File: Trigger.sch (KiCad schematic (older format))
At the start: 32 parts, among them J1 USB_B_Micro, J2 TP1, J3 Conn_01x04_IO, J4 Screw_Terminal_01x06, J5 Conn_01x05_Male, Q1 Q_NMOS_GSD, SW2 SW_Push, U1 MCP6002, U2 SAMD21E, U3 TPS769XX

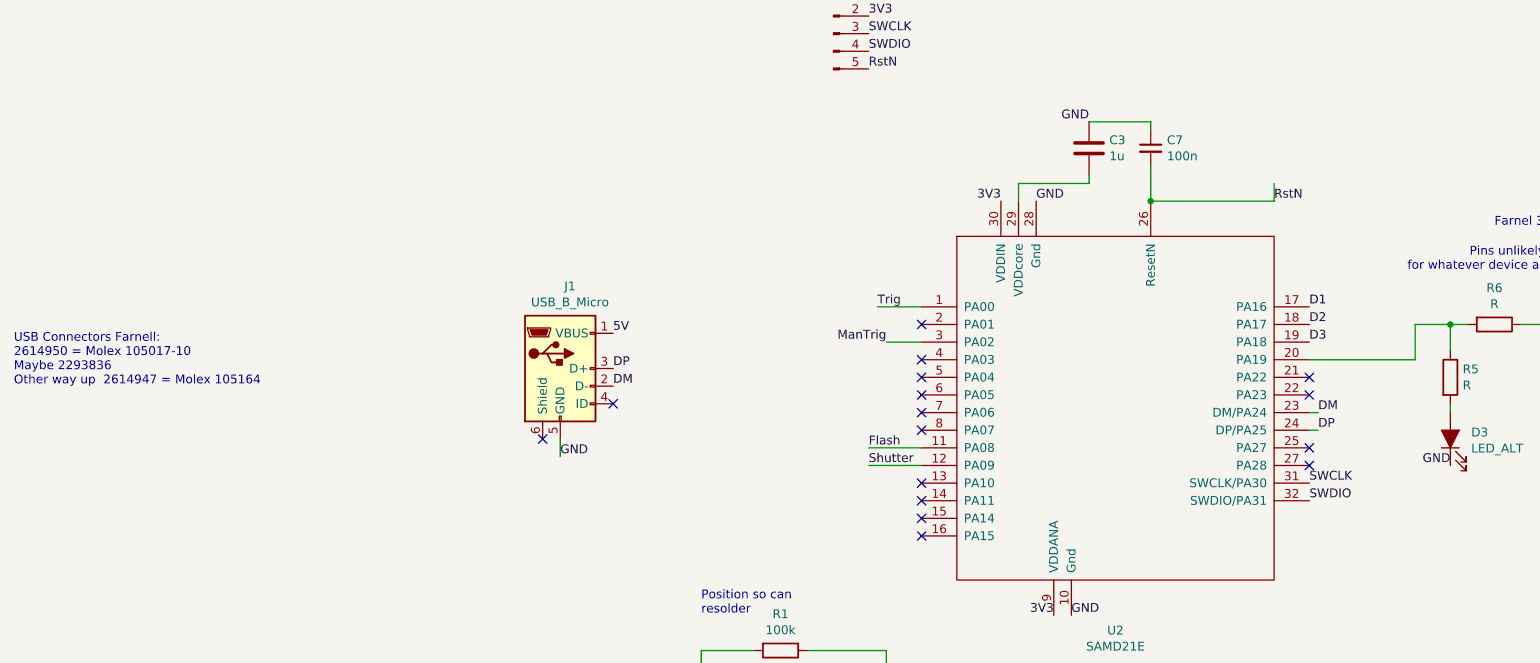
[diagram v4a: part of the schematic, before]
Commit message: Layout on board. Not in final positions
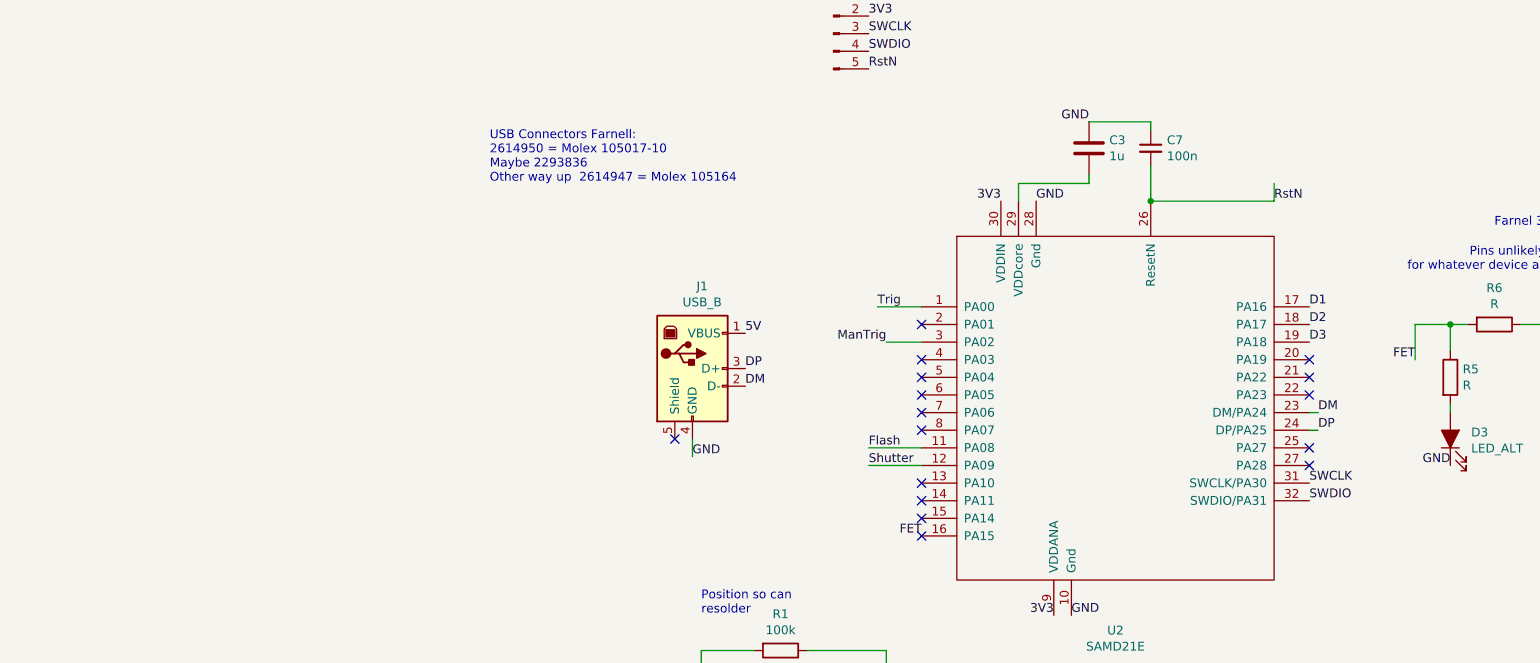
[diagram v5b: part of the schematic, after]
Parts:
- removed J1: USB_B_Micro, SMD_Mine:USB_B_Micro_47346-0001, symbol Connector:USB_B_Micro
- added J1: USB_B, SMD_Mine:USB_B_Micro_47346-0001, symbol Connector:USB_B
- C1: footprint Capacitor_SMD:C_0805_2012Metric -> Capacitors_SMD:C_0805_HandSoldering
- R1: footprint Resistor_SMD:R_0805_2012Metric -> Resistors_SMD:R_0805_HandSoldering
- R2, R4, R5, R6, R7: footprint Resistor_SMD:R_0805_2012Metric -> Resistors_SMD:R_0805
- RV1: footprint Resistor_SMD:R_0805_2012Metric -> SMD_Mine:Potentiometer_WirePads_largePads
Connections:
- net 5V: now also J1.1 (VBUS)
- net DM: now also J1.2 (D-)
- net DP: now also J1.3 (D+)
- net GND: now also J1.4 (GND)
- net FET: now reaches U2.16 (PA15)
- net FET: now also R5.1, R6.2
- now unconnected: U2.20 (PA19)
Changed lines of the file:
@@
 F 0 "C1" H 9942 2696 50  0000 R CNN
 F 1 "1u" H 9942 2605 50  0000 L CNN
-F 2 "Capacitor_SMD:C_0805_2012Metric" H 9850 2650 50  0001 C CNN
+F 2 "Capacitors_SMD:C_0805_HandSoldering" H 9850 2650 50  0001 C CNN
 F 3 "~" H 9850 2650 50  0001 C CNN
 	1    9850 2650
@@
 F 0 "R7" V 9943 850 50  0000 C CNN
 F 1 "10K" V 10034 850 50  0000 C CNN
-F 2 "Resistor_SMD:R_0805_2012Metric" V 10080 850 50  0001 C CNN
+F 2 "Resistors_SMD:R_0805" V 10080 850 50  0001 C CNN
 F 3 "~" H 10150 850 50  0001 C CNN
 	1    10150 850
@@
 	10400 1150 9900 1150
 Connection ~ 9900 1150
-$Comp
-L Connector:USB_B_Micro J1
-U 1 1 5C3A96B5
-P 1150 3600
-F 0 "J1" H 1205 4067 50  0000 C CNN
-F 1 "USB_B_Micro" H 1205 3976 50  0000 C CNN
-F 2 "SMD_Mine:USB_B_Micro_47346-0001" H 1300 3550 50  0001 C CNN
-F 3 "~" H 1300 3550 50  0001 C CNN
-	1    1150 3600
-	1    0    0    -1
-$EndComp
-Text Label 1450 3400 0    50   ~ 0
-5V
-Text Label 1150 4100 0    50   ~ 0
-GND
-Text Label 1450 3600 0    50   ~ 0
+Text Label 1900 4100 0    50   ~ 0
+GND
+Text Label 2200 3600 0    50   ~ 0
 DP
-Text Label 1450 3700 0    50   ~ 0
+Text Label 2200 3700 0    50   ~ 0
 DM
 Wire Wire Line
-	1150 4000 1150 4100
-NoConn ~ 1050 4000
-Text Notes -1950 3700 0    50   ~ 0
+	1900 4000 1900 4100
+NoConn ~ 1800 4000
+Text Notes 750  2550 0    50   ~ 0
 USB Connectors Farnell:\n2614950 = Molex 105017-10\nMaybe 2293836\nOther way up  2614947 = Molex 105164
 NoConn ~ 8350 850
@@
 F 0 "R1" V 2193 5200 50  0000 C CNN
 F 1 "100k" V 2284 5200 50  0000 C CNN
-F 2 "Resistor_SMD:R_0805_2012Metric" V 2330 5200 50  0001 C CNN
+F 2 "Resistors_SMD:R_0805_HandSoldering" V 2330 5200 50  0001 C CNN
 F 3 "~" H 2400 5200 50  0001 C CNN
 	1    2400 5200
@@
 F 0 "RV1" H 3580 6046 50  0000 R CNN
 F 1 "20k" H 3580 5955 50  0000 R CNN
-F 2 "Resistor_SMD:R_0805_2012Metric" H 3650 6000 50  0001 C CNN
+F 2 "SMD_Mine:Potentiometer_WirePads_largePads" H 3650 6000 50  0001 C CNN
 F 3 "~" H 3650 6000 50  0001 C CNN
 	1    3650 6000
@@
 F 0 "R4" V 5343 6200 50  0000 C CNN
 F 1 "220R" V 5434 6200 50  0000 C CNN
-F 2 "Resistor_SMD:R_0805_2012Metric" V 5480 6200 50  0001 C CNN
+F 2 "Resistors_SMD:R_0805" V 5480 6200 50  0001 C CNN
 F 3 "~" H 5550 6200 50  0001 C CNN
 	1    5550 6200
@@
 F 0 "R2" V 4143 5550 50  0000 C CNN
 F 1 "100k" V 4234 5550 50  0000 C CNN
-F 2 "Resistor_SMD:R_0805_2012Metric" V 4280 5550 50  0001 C CNN
+F 2 "Resistors_SMD:R_0805" V 4280 5550 50  0001 C CNN
 F 3 "~" H 4350 5550 50  0001 C CNN
 	1    4350 5550
@@
 F 0 "R6" V 6243 3350 50  0000 C CNN
 F 1 "R" V 6334 3350 50  0000 C CNN
-F 2 "Resistor_SMD:R_0805_2012Metric" V 6380 3350 50  0001 C CNN
+F 2 "Resistors_SMD:R_0805" V 6380 3350 50  0001 C CNN
 F 3 "~" H 6450 3350 50  0001 C CNN
 	1    6450 3350
@@
 F 0 "R5" H 6270 3696 50  0000 L CNN
 F 1 "R" H 6270 3605 50  0000 L CNN
-F 2 "Resistor_SMD:R_0805_2012Metric" V 6130 3650 50  0001 C CNN
+F 2 "Resistors_SMD:R_0805" V 6130 3650 50  0001 C CNN
 F 3 "~" H 6200 3650 50  0001 C CNN
 	1    6200 3650
@@
 Wire Wire Line
 	6000 3350 6200 3350
-Wire Wire Line
-	5400 3550 6000 3550
 Connection ~ 6200 3350
 Text Label 5400 3250 0    50   ~ 0
@@
 D3
 NoConn ~ 8650 850
-NoConn ~ 1450 3800
 NoConn ~ 3200 3350
 NoConn ~ 3200 3550
@@
 	1    0    0    -1
 $EndComp
+$Comp
+L Connector:USB_B J1
+U 1 1 5C462856
+P 1900 3600
+F 0 "J1" H 1955 4067 50  0000 C CNN
+F 1 "USB_B" H 1955 3976 50  0000 C CNN
+F 2 "SMD_Mine:USB_B_Micro_47346-0001" H 2050 3550 50  0001 C CNN
+F 3 " ~" H 2050 3550 50  0001 C CNN
+	1    1900 3600
+	1    0    0    -1
+$EndComp
+Text Label 2200 3400 0    50   ~ 0
+5V
+NoConn ~ 5400 3550
+Text Label 6000 3550 2    50   ~ 0
+FET
+Text Label 3200 4550 2    50   ~ 0
+FET
 $EndSCHEMATC

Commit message: Routed!
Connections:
- net Flash: now also J4.3 (Pin_3); no longer J4.4 (Pin_4)
- net Shutter: now also J4.4 (Pin_4); no longer J4.3 (Pin_3)
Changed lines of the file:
@@
 Text Label 8150 3200 0    50   ~ 0
 SW_FET
+Text Label 8150 3400 0    50   ~ 0
+Flash
 Text Label 8150 3300 0    50   ~ 0
-Flash
-Text Label 8150 3400 0    50   ~ 0
 Shutter
 $Comp
